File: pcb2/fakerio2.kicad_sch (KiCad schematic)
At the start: 10 parts, among them U1 LM7805_TO220, U2 MCP1700x-330xxTO

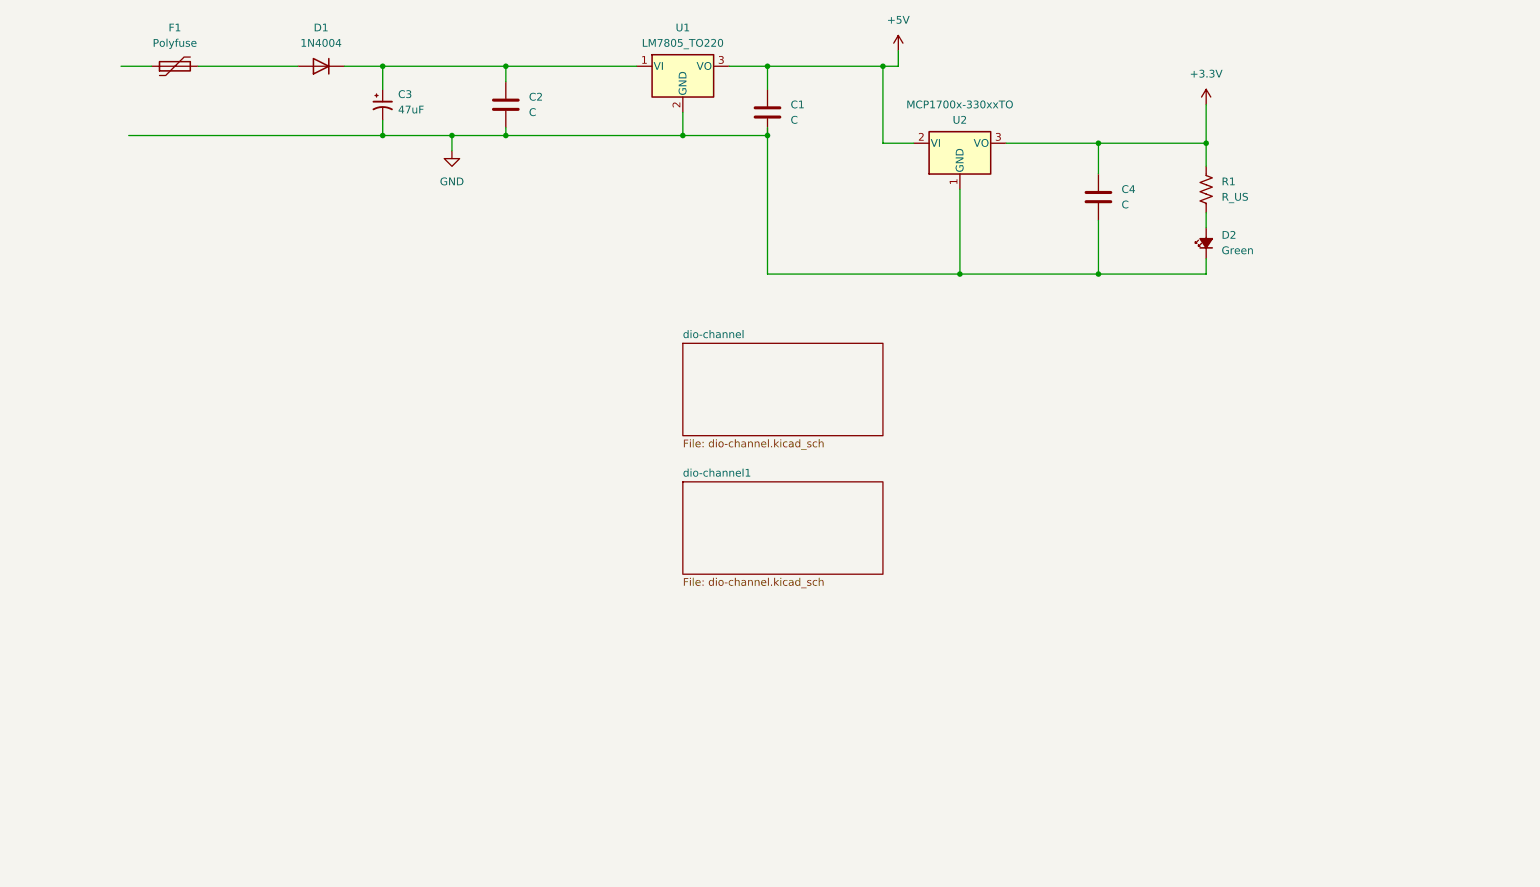
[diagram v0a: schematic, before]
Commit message: create fooprint for e-switch switch for SW1 etc get to a pretty good part placement, but want to try a variation
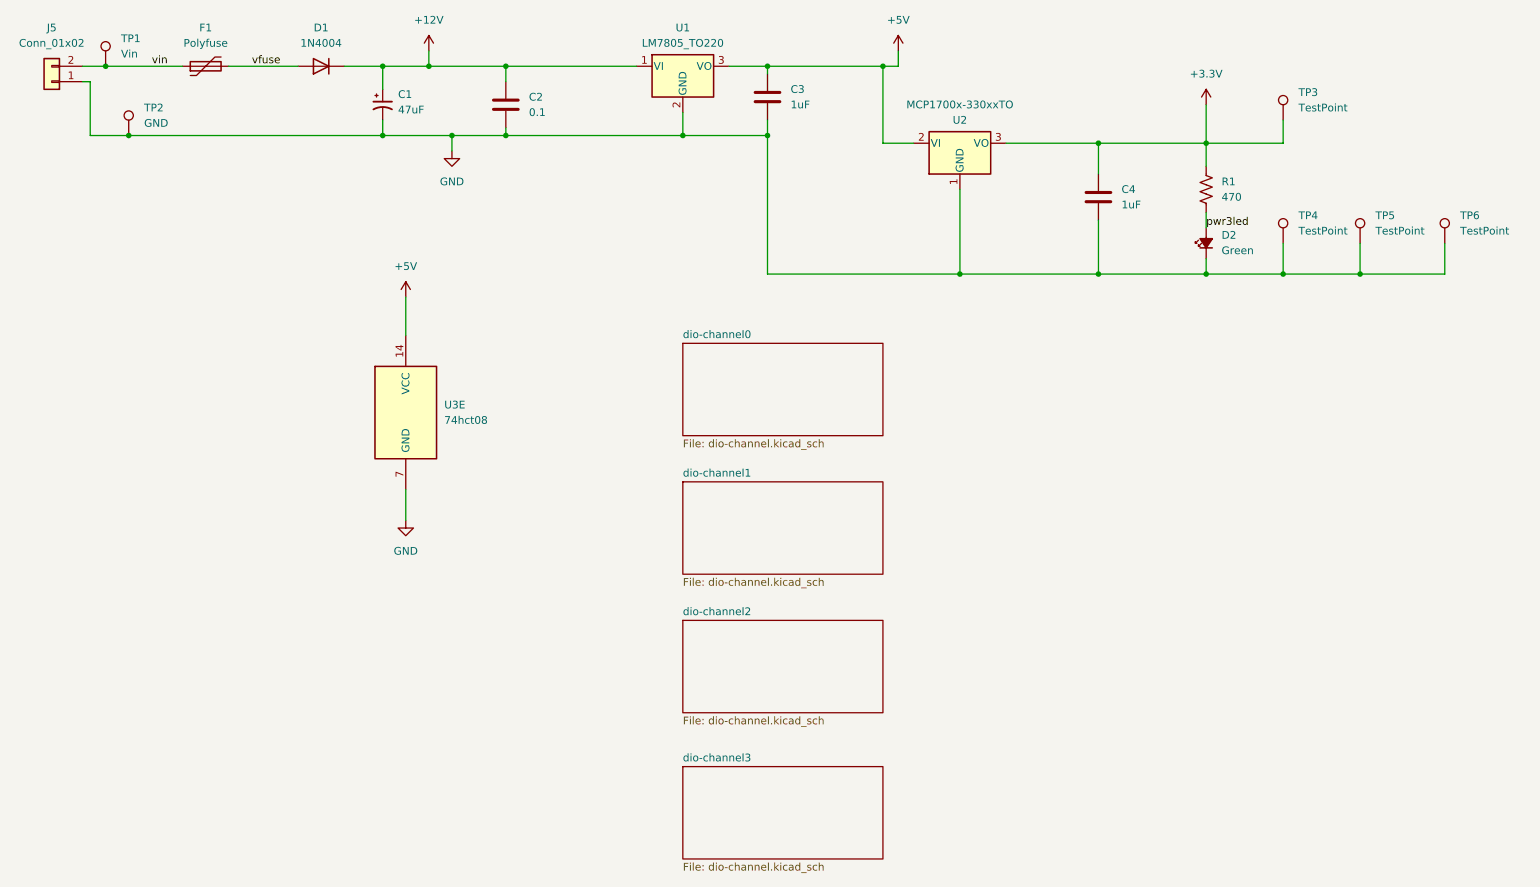
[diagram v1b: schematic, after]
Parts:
- added J5: Conn_01x02, Connector_PinHeader_2.54mm:PinHeader_1x02_P2.54mm_Vertical, symbol Connector_Generic:Conn_01x02
- added TP1: Vin, MountingHole:MountingHole_3mm_Pad_Via, symbol Connector:TestPoint
- added TP2: GND, MountingHole:MountingHole_3mm_Pad_Via, symbol Connector:TestPoint
- added TP3, TP4, TP5, TP6: TestPoint, Connector_PinHeader_2.54mm:PinHeader_1x01_P2.54mm_Vertical, symbol Connector:TestPoint
- added U3: 74hct08, Package_DIP:DIP-14_W7.62mm_Socket, symbol 74xx:74LS08
- C1: renamed from C3; footprint (none) -> Capacitor_THT:CP_Radial_D6.3mm_P2.50mm
- C2: value C -> 0.1; footprint (none) -> Capacitor_THT:C_Rect_L4.0mm_W2.5mm_P2.50mm
- C3: renamed from C1; value C -> 1uF; footprint (none) -> Capacitor_THT:C_Rect_L7.0mm_W4.5mm_P5.00mm
- C4: value C -> 1uF; footprint (none) -> Capacitor_THT:C_Rect_L7.0mm_W4.5mm_P5.00mm
- D2: footprint (none) -> LED_THT:LED_D5.0mm
- F1: footprint (none) -> Capacitor_THT:C_Disc_D11.0mm_W5.0mm_P5.00mm
- R1: value R_US -> 470; footprint (none) -> Resistor_THT:R_Axial_DIN0207_L6.3mm_D2.5mm_P10.16mm_Horizontal
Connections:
- net +3.3V: now also TP3.1
- net +5V: now also U3.14 (VCC)
- net GND: now also J5.1 (Pin_1), TP2.1, TP4.1, TP5.1, TP6.1, U3.7 (GND)
- net vin: now reaches F1.1
- net vin: now also J5.2 (Pin_2), TP1.1
- net vfuse: now reaches D1.2 (A), F1.2
- net +12V: now reaches C1.1, C2.1, D1.1 (K), U1.1 (VI)
- net pwr3led: now reaches D2.2 (A), R1.2
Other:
- sheet dio-channel renamed dio-channel0
- added sheet dio-channel2 (dio-channel.kicad_sch)
- added sheet dio-channel3 (dio-channel.kicad_sch)
- moved on the sheet: C3, F1
